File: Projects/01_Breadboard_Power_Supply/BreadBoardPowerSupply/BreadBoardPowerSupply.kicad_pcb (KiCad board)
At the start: 2 copper layers, 15 parts, among them J1 Barrel_Jack_Switch, J2 Conn_02x02_Odd_Even, J3 Conn_02x02_Odd_Even, SW1 SW_DPDT_x2, U1 LM7805_TO220

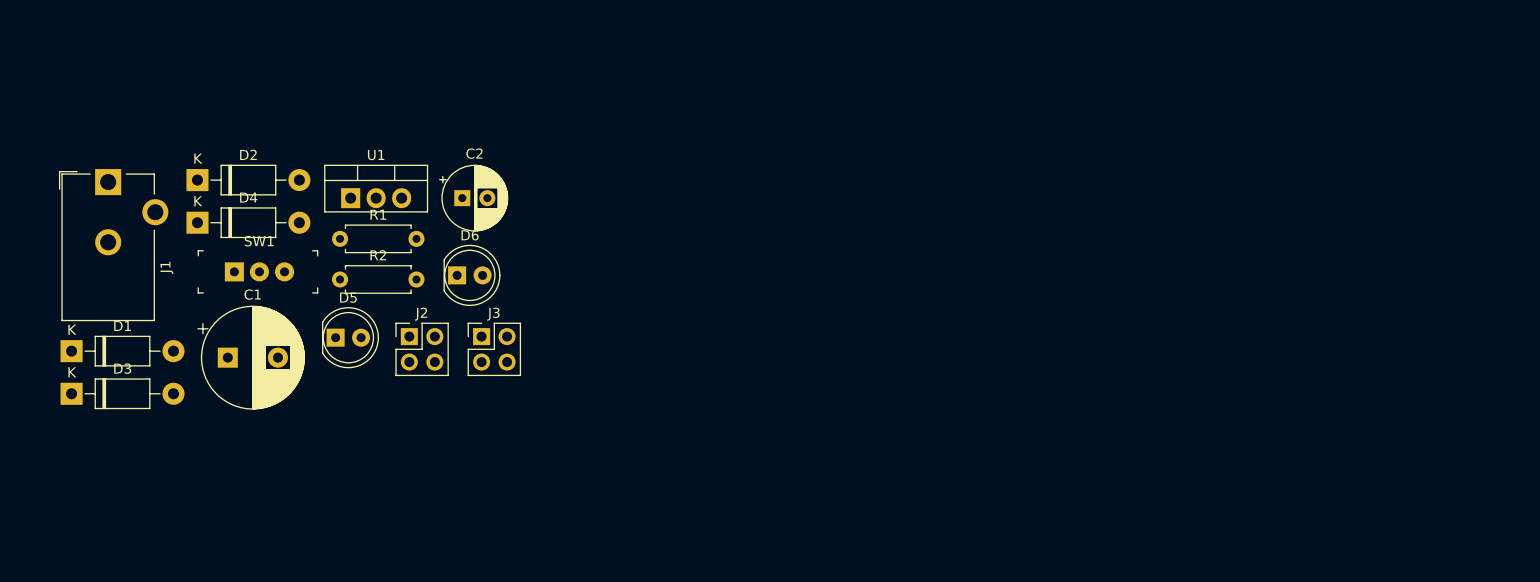
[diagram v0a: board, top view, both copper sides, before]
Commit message: Define size and shape of PCB edgecut layer
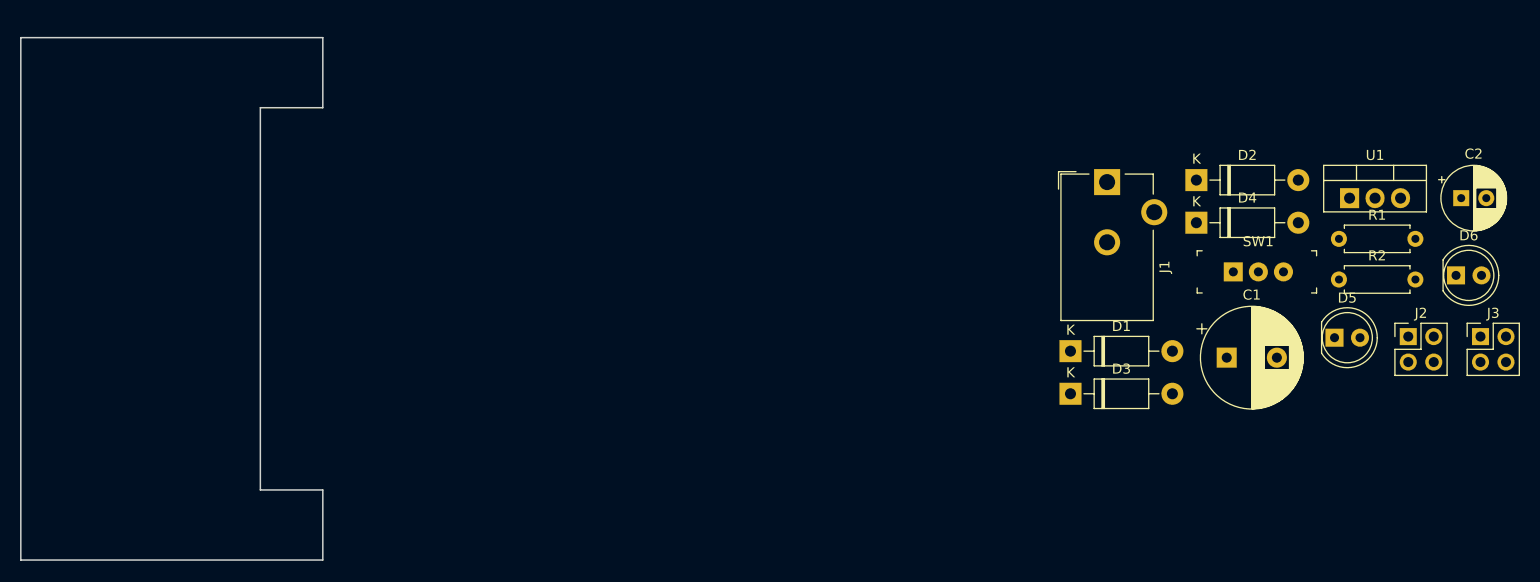
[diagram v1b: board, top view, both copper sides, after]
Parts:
- moved C1 99.6 mm to (243.5, 104.4)
- moved D1 99.6 mm to (227.9, 103.8)
- moved D3 99.6 mm to (227.9, 108.0)
- moved D5 99.6 mm to (254.3, 102.4)
- moved R1 99.6 mm to (254.7, 92.6)
- moved R2 99.6 mm to (254.7, 96.6)
- moved SW1 99.6 mm to (244.2, 95.9)
- moved U1 99.6 mm to (255.8, 88.5)
- moved C2 99.6 mm to (266.9, 88.5)
- moved D2 99.6 mm to (240.5, 86.7)
- moved D4 99.6 mm to (240.5, 91.0)
- moved D6 99.6 mm to (266.4, 96.2)
- moved J1 99.6 mm to (231.6, 86.9)
- moved J2 99.6 mm to (261.6, 102.3)
- moved J3 99.6 mm to (268.8, 102.3)
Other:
- board outline added: 30.1 x 52.1 mm

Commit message: Place components on board: 	- Arrange user interface components 	- Arrange in functional blocks 	- Complete placement
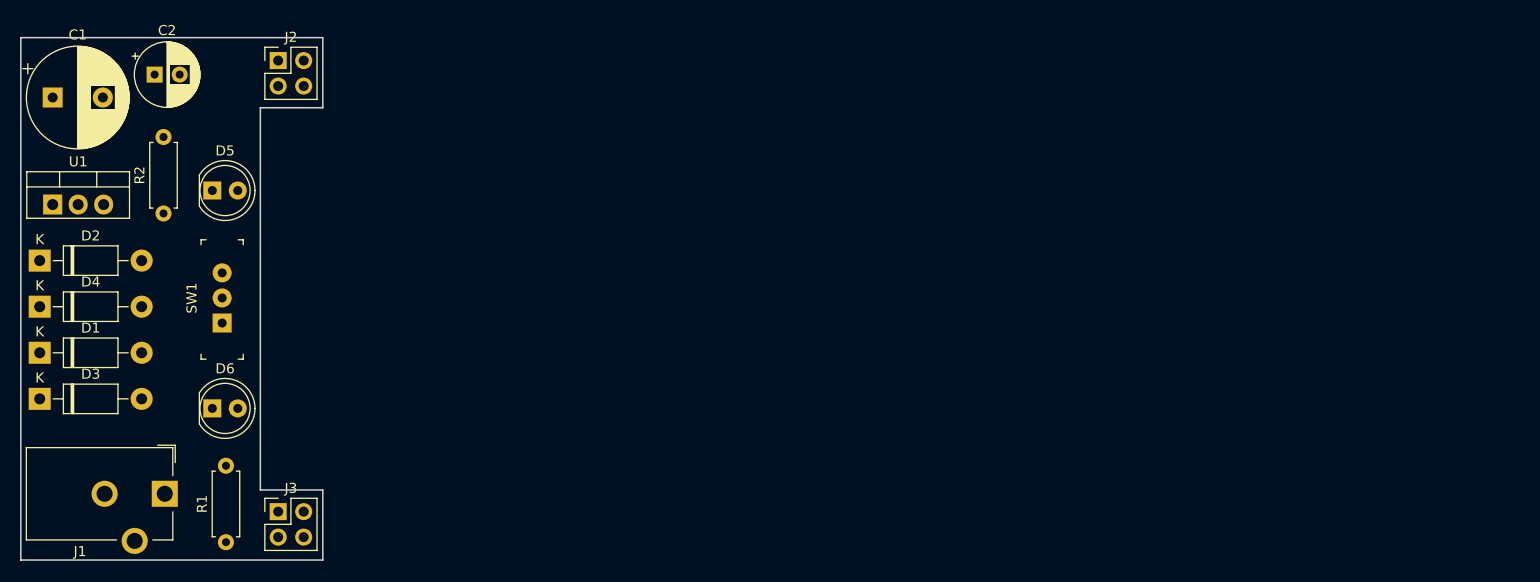
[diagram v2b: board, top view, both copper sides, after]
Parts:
- moved C2 130.8 mm to (136.7, 76.2)
- moved U1 129.3 mm to (126.5, 89.2)
- moved D6 124.7 mm to (142.4, 109.5)
- moved J3 121.1 mm to (149.0, 119.8)
- moved C1 119.9 mm to (126.5, 78.5)
- moved R2 117.3 mm to (137.5, 90.0), turned to 90 degrees
- moved J2 116.0 mm to (149.0, 74.8)
- moved D4 115.6 mm to (125.2, 99.3)
- moved D2 115.6 mm to (125.2, 94.7)
- moved R1 115.0 mm to (143.8, 122.8), turned to 90 degrees
- moved D5 112.8 mm to (142.4, 87.8)
- moved D3 102.7 mm to (125.2, 108.5)
- moved D1 102.7 mm to (125.2, 103.9)
- moved SW1 100.9 mm to (143.4, 101.0), turned to 90 degrees
- moved J1 98.9 mm to (137.7, 118.0), turned to 270 degrees

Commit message: Connect all V- traces on B.Cu
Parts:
- moved D5 21.7 mm to (142.4, 109.5)
- moved D6 21.6 mm to (142.4, 87.9)
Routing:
- net /V-: track 0.00 -> 87.4 mm
- net Net-(D3-Pad2): track 0.00 -> 25.0 mm
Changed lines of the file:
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@@
     (thickness 1.6)
     (drawings 8)
-    (tracks 0)
+    (tracks 26)
     (zones 0)
     (modules 15)
@@
   )
   (setup
-    (last_trace_width 0.25)
+    (last_trace_width 0.3)
     (user_trace_width 0.3)
     (trace_clearance 0.2)
@@
     (uvia_drill 0.1)
     (add_net "Net-(D1-Pad2)")
-    (add_net "Net-(D3-Pad2)")
     (add_net "Net-(D5-Pad2)")
     (add_net "Net-(D6-Pad2)")
@@
     (add_net /Vout1)
     (add_net /Vout2)
+    (add_net "Net-(D3-Pad2)")
   )
   (module Capacitor_THT:CP_Radial_D10.0mm_P5.00mm (layer F.Cu)
@@
     )
   )
-  (module LED_THT:LED_D5.0mm locked (layer F.Cu)
-    (at 142.403 87.757)
+  (module LED_THT:LED_D5.0mm (layer F.Cu)
+    (at 142.403 109.474)
     (descr "LED, diameter 5.0mm, 2 pins, http://cdn-reichelt.de/documents/datenblatt/A500/LL-504BC2E-009.pdf")
     (tags "LED diameter 5.0mm 2 pins")
@@
     )
   )
-  (module LED_THT:LED_D5.0mm locked (layer F.Cu)
-    (at 142.403 109.474)
+  (module LED_THT:LED_D5.0mm (layer F.Cu)
+    (at 142.403 87.884)
     (descr "LED, diameter 5.0mm, 2 pins, http://cdn-reichelt.de/documents/datenblatt/A500/LL-504BC2E-009.pdf")
     (tags "LED diameter 5.0mm 2 pins")
@@
   (gr_line (start 123.317 124.587) (end 153.416 124.587) (layer Edge.Cuts) (width 0.15))
   (gr_line (start 123.317 72.517) (end 123.317 124.587) (layer Edge.Cuts) (width 0.15))
+  (segment (start 126.750002 89.412002) (end 126.492 89.154) (width 0.3) (layer F.Cu) (net 1))
+  (segment (start 135.360001 99.335667) (end 135.360001 94.742) (width 0.3) (layer B.Cu) (net 2))
+  (segment (start 142.345001 87.757) (end 142.403 87.757) (width 0.3) (layer B.Cu) (net 2))
+  (segment (start 129.254502 89.154) (end 129.032 89.154) (width 0.3) (layer B.Cu) (net 2))
+  (segment (start 134.842502 94.742) (end 129.254502 89.154) (width 0.3) (layer B.Cu) (net 2))
+  (segment (start 135.360001 94.742) (end 134.842502 94.742) (width 0.3) (layer B.Cu) (net 2))
+  (segment (start 129.032 80.946) (end 131.492 78.486) (width 0.3) (layer B.Cu) (net 2))
+  (segment (start 129.032 89.154) (end 129.032 80.946) (width 0.3) (layer B.Cu) (net 2))
+  (segment (start 139.062002 76.2) (end 139.152 76.2) (width 0.3) (layer B.Cu) (net 2))
+  (segment (start 136.776002 78.486) (end 139.062002 76.2) (width 0.3) (layer B.Cu) (net 2))
+  (segment (start 131.492 78.486) (end 136.776002 78.486) (width 0.3) (layer B.Cu) (net 2))
+  (segment (start 147.828 76.2) (end 148.971 77.343) (width 0.3) (layer B.Cu) (net 2))
+  (segment (start 139.152 76.2) (end 147.828 76.2) (width 0.3) (layer B.Cu) (net 2))
+  (segment (start 148.971 77.343) (end 151.511 77.343) (width 0.3) (layer B.Cu) (net 2))
+  (segment (start 148.971 122.301) (end 151.511 122.301) (width 0.3) (layer B.Cu) (net 2))
+  (segment (start 146.66799 113.73899) (end 142.403 109.474) (width 0.3) (layer B.Cu) (net 2))
+  (segment (start 146.66799 119.99799) (end 146.66799 113.73899) (width 0.3) (layer B.Cu) (net 2))
+  (segment (start 148.971 122.301) (end 146.66799 119.99799) (width 0.3) (layer B.Cu) (net 2))
+  (segment (start 142.403 106.378666) (end 135.360001 99.335667) (width 0.3) (layer B.Cu) (net 2))
+  (segment (start 142.403 109.474) (end 142.403 106.378666) (width 0.3) (layer B.Cu) (net 2))
+  (segment (start 142.218001 87.884) (end 142.403 87.884) (width 0.3) (layer B.Cu) (net 2))
+  (segment (start 135.360001 94.742) (end 142.218001 87.884) (width 0.3) (layer B.Cu) (net 2))
+  (segment (start 131.668 112.215002) (end 135.360001 108.523001) (width 0.3) (layer B.Cu) (net 5))
+  (segment (start 131.668 117.983) (end 131.668 112.215002) (width 0.3) (layer B.Cu) (net 5))
+  (segment (start 126.172667 99.335667) (end 125.200001 99.335667) (width 0.3) (layer B.Cu) (net 5))
+  (segment (start 135.360001 108.523001) (end 126.172667 99.335667) (width 0.3) (layer B.Cu) (net 5))
 )
